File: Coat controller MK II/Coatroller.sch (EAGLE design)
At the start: 3 parts, among them U1 ATMEGA328P_PDIP, U2 V_REG_LDOSMD, Y1 ABM3B-16.000MHZ-B2-T

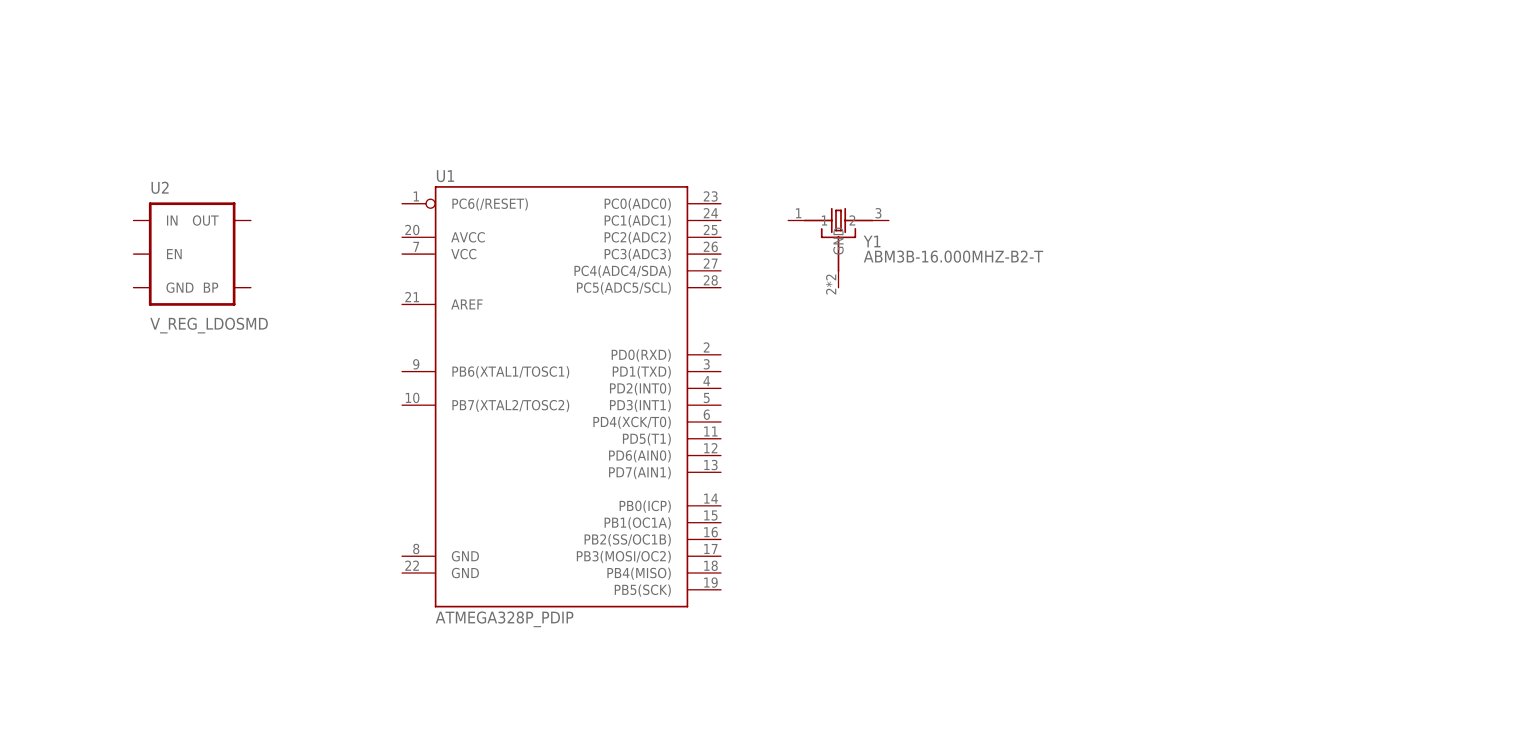
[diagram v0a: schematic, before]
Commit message: added more parts
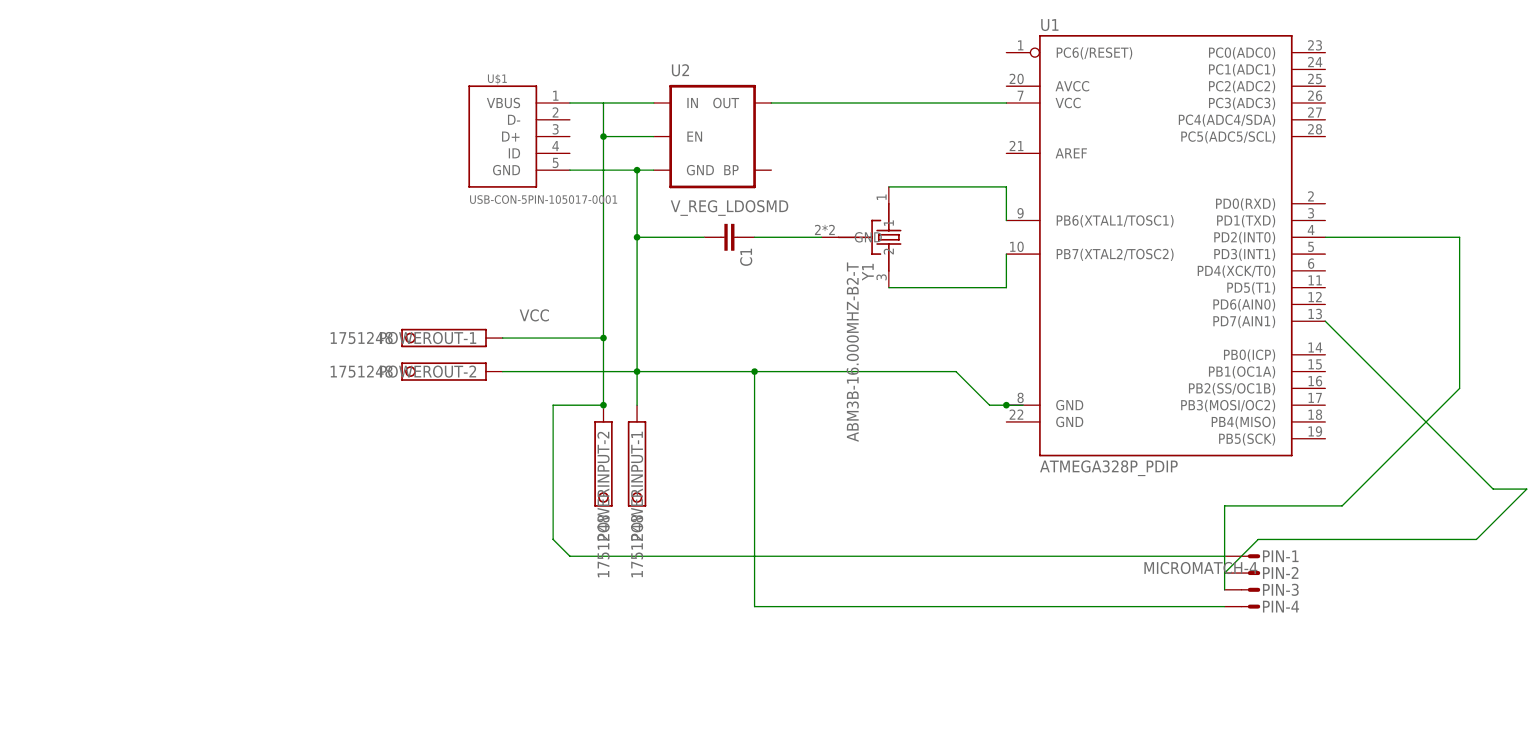
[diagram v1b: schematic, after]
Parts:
- added C1: (no value), SparkFun-Capacitors:2.2UF50V10%(1206)
- added PIN: MICROMATCH-4, con-amp-micromatch:MICROMATCH-4
- added POWERINPUT, POWEROUT: 1751248, con-phoenix-350:1751248
- added U$1: USB-CON-5PIN-105017-0001, GeekAmmo:USB-CON-5PIN-105017-0001
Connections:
- new net 5V: U1.VCC, U2.OUT
- new net GROUND: C1.2, PIN-4.S, POWERINPUT-1.K, POWEROUT-2.K, U$1.GND, U1.GND@1, U2.GND
- new net N$1: U1.PB6(XTAL1/TOSC1), Y1.1
- new net N$2: U1.PB7(XTAL2/TOSC2), Y1.2
- new net N$3: C1.1, Y1.GND
- new net N$4: PIN-3.S, U1.PD7(AIN1)
- new net N$5: PIN-2.S, U1.PD2(INT0)
- new net VCC: PIN-1.S, POWERINPUT-2.K, POWEROUT-1.K, U$1.VBUS, U2.EN, U2.IN
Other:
- moved on the sheet: U1, U2, Y1

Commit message: finished placing and routing
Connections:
- removed net N$4: PIN-3.S, U1.PD7(AIN1)
- removed net N$5: PIN-2.S, U1.PD2(INT0)
- new net CLOCK: PIN-3.S, U1.PD4(XCK/T0)
- new net DATA: PIN-2.S, U1.PD7(AIN1)
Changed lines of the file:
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@@
 <?xml version="1.0" encoding="utf-8"?>
 <!DOCTYPE eagle SYSTEM "eagle.dtd">
-<eagle version="7.5.0">
+<eagle version="7.6.0">
 <drawing>
 <settings>
@@
 <grid distance="0.1" unitdist="inch" unit="inch" style="lines" multiple="1" display="no" altdistance="0.01" altunitdist="inch" altunit="inch"/>
 <layers>
-<layer number="1" name="Top" color="4" fill="1" visible="yes" active="no"/>
-<layer number="16" name="Bottom" color="1" fill="1" visible="yes" active="no"/>
-<layer number="17" name="Pads" color="2" fill="1" visible="yes" active="no"/>
-<layer number="18" name="Vias" color="2" fill="1" visible="yes" active="no"/>
-<layer number="19" name="Unrouted" color="6" fill="1" visible="yes" active="no"/>
-<layer number="20" name="Dimension" color="15" fill="1" visible="yes" active="no"/>
-<layer number="21" name="tPlace" color="16" fill="1" visible="yes" active="no"/>
-<layer number="22" name="bPlace" color="14" fill="1" visible="yes" active="no"/>
-<layer number="23" name="tOrigins" color="15" fill="1" visible="yes" active="no"/>
-<layer number="24" name="bOrigins" color="15" fill="1" visible="yes" active="no"/>
-<layer number="25" name="tNames" color="7" fill="1" visible="yes" active="no"/>
-<layer number="26" name="bNames" color="7" fill="1" visible="yes" active="no"/>
-<layer number="27" name="tValues" color="7" fill="1" visible="yes" active="no"/>
-<layer number="28" name="bValues" color="7" fill="1" visible="yes" active="no"/>
+<layer number="1" name="Top" color="4" fill="1" visible="no" active="no"/>
+<layer number="16" name="Bottom" color="1" fill="1" visible="no" active="no"/>
+<layer number="17" name="Pads" color="2" fill="1" visible="no" active="no"/>
+<layer number="18" name="Vias" color="2" fill="1" visible="no" active="no"/>
+<layer number="19" name="Unrouted" color="6" fill="1" visible="no" active="no"/>
+<layer number="20" name="Dimension" color="15" fill="1" visible="no" active="no"/>
+<layer number="21" name="tPlace" color="16" fill="1" visible="no" active="no"/>
+<layer number="22" name="bPlace" color="14" fill="1" visible="no" active="no"/>
+<layer number="23" name="tOrigins" color="15" fill="1" visible="no" active="no"/>
+<layer number="24" name="bOrigins" color="15" fill="1" visible="no" active="no"/>
+<layer number="25" name="tNames" color="7" fill="1" visible="no" active="no"/>
+<layer number="26" name="bNames" color="7" fill="1" visible="no" active="no"/>
+<layer number="27" name="tValues" color="7" fill="1" visible="no" active="no"/>
+<layer number="28" name="bValues" color="7" fill="1" visible="no" active="no"/>
 <layer number="29" name="tStop" color="7" fill="3" visible="no" active="no"/>
 <layer number="30" name="bStop" color="7" fill="6" visible="no" active="no"/>
@@
 <layer number="35" name="tGlue" color="7" fill="4" visible="no" active="no"/>
 <layer number="36" name="bGlue" color="7" fill="5" visible="no" active="no"/>
-<layer number="37" name="tTest" color="7" fill="1" visible="yes" active="no"/>
-<layer number="38" name="bTest" color="7" fill="1" visible="yes" active="no"/>
+<layer number="37" name="tTest" color="7" fill="1" visible="no" active="no"/>
+<layer number="38" name="bTest" color="7" fill="1" visible="no" active="no"/>
 <layer number="39" name="tKeepout" color="4" fill="11" visible="no" active="no"/>
 <layer number="40" name="bKeepout" color="1" fill="11" visible="no" active="no"/>
@@
 <layer number="44" name="Drills" color="7" fill="1" visible="no" active="no"/>
 <layer number="45" name="Holes" color="7" fill="1" visible="no" active="no"/>
-<layer number="46" name="Milling" color="3" fill="1" visible="yes" active="no"/>
-<layer number="47" name="Measures" color="7" fill="1" visible="yes" active="no"/>
-<layer number="48" name="Document" color="7" fill="1" visible="yes" active="no"/>
-<layer number="49" name="Reference" color="7" fill="1" visible="yes" active="no"/>
-<layer number="50" name="dxf" color="7" fill="1" visible="yes" active="no"/>
-<layer number="51" name="tDocu" color="6" fill="1" visible="yes" active="no"/>
-<layer number="52" name="bDocu" color="7" fill="1" visible="yes" active="no"/>
-<layer number="53" name="tGND_GNDA" color="7" fill="9" visible="yes" active="no"/>
-<layer number="54" name="bGND_GNDA" color="1" fill="9" visible="yes" active="no"/>
-<layer number="56" name="wert" color="7" fill="1" visible="yes" active="no"/>
-<layer number="57" name="tCAD" color="7" fill="1" visible="yes" active="no"/>
-<layer number="59" name="tCarbon" color="7" fill="1" visible="yes" active="no"/>
-<layer number="60" name="bCarbon" color="7" fill="1" visible="yes" active="no"/>
+<layer number="46" name="Milling" color="3" fill="1" visible="no" active="no"/>
+<layer number="47" name="Measures" color="7" fill="1" visible="no" active="no"/>
+<layer number="48" name="Document" color="7" fill="1" visible="no" active="no"/>
+<layer number="49" name="Reference" color="7" fill="1" visible="no" active="no"/>
+<layer number="50" name="dxf" color="7" fill="1" visible="no" active="no"/>
+<layer number="51" name="tDocu" color="6" fill="1" visible="no" active="no"/>
+<layer number="52" name="bDocu" color="7" fill="1" visible="no" active="no"/>
+<layer number="53" name="tGND_GNDA" color="7" fill="9" visible="no" active="no"/>
+<layer number="54" name="bGND_GNDA" color="1" fill="9" visible="no" active="no"/>
+<layer number="56" name="wert" color="7" fill="1" visible="no" active="no"/>
+<layer number="57" name="tCAD" color="7" fill="1" visible="no" active="no"/>
+<layer number="59" name="tCarbon" color="7" fill="1" visible="no" active="no"/>
+<layer number="60" name="bCarbon" color="7" fill="1" visible="no" active="no"/>
 <layer number="90" name="Modules" color="5" fill="1" visible="yes" active="yes"/>
 <layer number="91" name="Nets" color="2" fill="1" visible="yes" active="yes"/>
@@
 <schematic xreflabel="%F%N/%S.%C%R" xrefpart="/%S.%C%R">
 <description>still needs:
-1.correct micromatch output
 2.on/off switch
 4.status LED
-5. bluetooth?
-6. pattern button</description>
+Pattern button will be moved to the sleeve.</description>
 <attributes>
 </attributes>
@@
 <wire x1="50.8" y1="55.88" x2="58.42" y2="55.88" width="0.1524" layer="91"/>
 <junction x="58.42" y="55.88"/>
+<label x="114.3" y="35.56" size="1.778" layer="95"/>
 </segment>
 </net>
@@
 </segment>
 </net>
-<net name="N$5" class="0">
+<net name="DATA" class="0">
 <segment>
 <pinref part="PIN" gate="-2" pin="S"/>
-<wire x1="152.4" y1="30.48" x2="152.4" y2="40.64" width="0.1524" layer="91"/>
-<wire x1="152.4" y1="40.64" x2="170.18" y2="40.64" width="0.1524" layer="91"/>
-<wire x1="170.18" y1="40.64" x2="187.96" y2="58.42" width="0.1524" layer="91"/>
-<wire x1="187.96" y1="58.42" x2="187.96" y2="81.28" width="0.1524" layer="91"/>
-<pinref part="U1" gate="G$1" pin="PD2(INT0)"/>
-<wire x1="187.96" y1="81.28" x2="167.64" y2="81.28" width="0.1524" layer="91"/>
-</segment>
-</net>
-<net name="N$4" class="0">
+<wire x1="152.4" y1="30.48" x2="152.4" y2="35.56" width="0.1524" layer="91"/>
+<wire x1="152.4" y1="35.56" x2="154.94" y2="38.1" width="0.1524" layer="91"/>
+<wire x1="154.94" y1="38.1" x2="175.26" y2="38.1" width="0.1524" layer="91"/>
+<wire x1="175.26" y1="38.1" x2="175.26" y2="68.58" width="0.1524" layer="91"/>
+<pinref part="U1" gate="G$1" pin="PD7(AIN1)"/>
+<wire x1="175.26" y1="68.58" x2="167.64" y2="68.58" width="0.1524" layer="91"/>
+</segment>
+</net>
+<net name="CLOCK" class="0">
 <segment>
 <pinref part="PIN" gate="-3" pin="S"/>
-<wire x1="152.4" y1="27.94" x2="152.4" y2="30.48" width="0.1524" layer="91"/>
-<wire x1="152.4" y1="30.48" x2="157.48" y2="35.56" width="0.1524" layer="91"/>
-<wire x1="157.48" y1="35.56" x2="190.5" y2="35.56" width="0.1524" layer="91"/>
-<wire x1="190.5" y1="35.56" x2="198.12" y2="43.18" width="0.1524" layer="91"/>
-<pinref part="U1" gate="G$1" pin="PD7(AIN1)"/>
-<wire x1="198.12" y1="43.18" x2="193.04" y2="43.18" width="0.1524" layer="91"/>
-<wire x1="193.04" y1="43.18" x2="167.64" y2="68.58" width="0.1524" layer="91"/>
-</segment>
-</net>
+<wire x1="152.4" y1="27.94" x2="147.32" y2="27.94" width="0.1524" layer="91"/>
+<wire x1="147.32" y1="27.94" x2="147.32" y2="43.18" width="0.1524" layer="91"/>
+<wire x1="147.32" y1="43.18" x2="182.88" y2="43.18" width="0.1524" layer="91"/>
+<wire x1="182.88" y1="43.18" x2="182.88" y2="76.2" width="0.1524" layer="91"/>
+<pinref part="U1" gate="G$1" pin="PD4(XCK/T0)"/>
+<wire x1="182.88" y1="76.2" x2="167.64" y2="76.2" width="0.1524" layer="91"/>
+</segment>
+</net>

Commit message: Fixed crystal and caps
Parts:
- added C2: (no value), SparkFun-Capacitors:2.2UF50V10%(1206)
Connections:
- removed net N$3: C1.1, Y1.GND
- net GROUND: now also C2.2, Y1.GND
- net N$1: now also C1.1
- net N$2: now also C2.1
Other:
- moved on the sheet: C1
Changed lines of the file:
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@@
 <?xml version="1.0" encoding="utf-8"?>
 <!DOCTYPE eagle SYSTEM "eagle.dtd">
-<eagle version="7.6.0">
+<eagle version="7.5.0">
 <drawing>
 <settings>
@@
 <part name="C1" library="SparkFun-Capacitors" deviceset="2.2UF50V10%(1206)" device=""/>
 <part name="PIN" library="con-amp-micromatch" deviceset="MICROMATCH-4" device=""/>
+<part name="C2" library="SparkFun-Capacitors" deviceset="2.2UF50V10%(1206)" device=""/>
 </parts>
 <sheets>
@@
 <instance part="POWEROUT" gate="-1" x="40.64" y="66.04" rot="R180"/>
 <instance part="POWEROUT" gate="-2" x="40.64" y="60.96" rot="R180"/>
-<instance part="C1" gate="G$1" x="76.2" y="81.28" rot="R270"/>
+<instance part="C1" gate="G$1" x="88.9" y="88.9" rot="R270"/>
 <instance part="PIN" gate="-1" x="157.48" y="33.02" rot="R180"/>
 <instance part="PIN" gate="-2" x="157.48" y="30.48" rot="R180"/>
 <instance part="PIN" gate="-3" x="157.48" y="27.94" rot="R180"/>
 <instance part="PIN" gate="-4" x="157.48" y="25.4" rot="R180"/>
+<instance part="C2" gate="G$1" x="88.9" y="73.66" rot="R270"/>
 </instances>
 <busses>
@@
 <pinref part="POWERINPUT" gate="-1" pin="K"/>
 <wire x1="63.5" y1="55.88" x2="63.5" y2="60.96" width="0.1524" layer="91"/>
-<wire x1="63.5" y1="60.96" x2="63.5" y2="81.28" width="0.1524" layer="91"/>
 <pinref part="POWEROUT" gate="-2" pin="K"/>
-<wire x1="63.5" y1="81.28" x2="63.5" y2="91.44" width="0.1524" layer="91"/>
+<wire x1="63.5" y1="60.96" x2="63.5" y2="78.74" width="0.1524" layer="91"/>
+<wire x1="63.5" y1="78.74" x2="63.5" y2="81.28" width="0.1524" layer="91"/>
+<wire x1="63.5" y1="81.28" x2="63.5" y2="83.82" width="0.1524" layer="91"/>
+<wire x1="63.5" y1="83.82" x2="63.5" y2="91.44" width="0.1524" layer="91"/>
 <wire x1="63.5" y1="60.96" x2="43.18" y2="60.96" width="0.1524" layer="91"/>
 <junction x="63.5" y="60.96"/>
@@
 <pinref part="U1" gate="G$1" pin="GND@1"/>
 <junction x="119.38" y="55.88"/>
-<pinref part="C1" gate="G$1" pin="2"/>
 <wire x1="81.28" y1="60.96" x2="63.5" y2="60.96" width="0.1524" layer="91"/>
-<wire x1="73.66" y1="81.28" x2="63.5" y2="81.28" width="0.1524" layer="91"/>
-<junction x="63.5" y="81.28"/>
 <pinref part="PIN" gate="-4" pin="S"/>
 <wire x1="152.4" y1="25.4" x2="81.28" y2="25.4" width="0.1524" layer="91"/>
 <wire x1="81.28" y1="25.4" x2="81.28" y2="60.96" width="0.1524" layer="91"/>
 <junction x="81.28" y="60.96"/>
+<pinref part="C1" gate="G$1" pin="2"/>
+<wire x1="86.36" y1="88.9" x2="83.82" y2="88.9" width="0.1524" layer="91"/>
+<wire x1="83.82" y1="88.9" x2="83.82" y2="83.82" width="0.1524" layer="91"/>
+<wire x1="83.82" y1="83.82" x2="63.5" y2="83.82" width="0.1524" layer="91"/>
+<junction x="63.5" y="83.82"/>
+<pinref part="C2" gate="G$1" pin="2"/>
+<wire x1="86.36" y1="73.66" x2="83.82" y2="73.66" width="0.1524" layer="91"/>
+<wire x1="83.82" y1="73.66" x2="83.82" y2="78.74" width="0.1524" layer="91"/>
+<wire x1="83.82" y1="78.74" x2="63.5" y2="78.74" width="0.1524" layer="91"/>
+<junction x="63.5" y="78.74"/>
+<pinref part="Y1" gate="G$1" pin="GND"/>
+<wire x1="91.44" y1="81.28" x2="63.5" y2="81.28" width="0.1524" layer="91"/>
+<junction x="63.5" y="81.28"/>
 </segment>
 </net>
@@
 <wire x1="101.6" y1="88.9" x2="119.38" y2="88.9" width="0.1524" layer="91"/>
 <wire x1="119.38" y1="88.9" x2="119.38" y2="83.82" width="0.1524" layer="91"/>
+<pinref part="C1" gate="G$1" pin="1"/>
+<wire x1="101.6" y1="88.9" x2="93.98" y2="88.9" width="0.1524" layer="91"/>
+<junction x="101.6" y="88.9"/>
 </segment>
 </net>
@@
 <wire x1="101.6" y1="73.66" x2="119.38" y2="73.66" width="0.1524" layer="91"/>
 <wire x1="119.38" y1="73.66" x2="119.38" y2="78.74" width="0.1524" layer="91"/>
-</segment>
-</net>
-<net name="N$3" class="0">
-<segment>
-<pinref part="Y1" gate="G$1" pin="GND"/>
-<pinref part="C1" gate="G$1" pin="1"/>
-<wire x1="91.44" y1="81.28" x2="81.28" y2="81.28" width="0.1524" layer="91"/>
-</segment>
-</net>
+<pinref part="C2" gate="G$1" pin="1"/>
+<wire x1="101.6" y1="73.66" x2="93.98" y2="73.66" width="0.1524" layer="91"/>
+<junction x="101.6" y="73.66"/>
+</segment>
+</net>
